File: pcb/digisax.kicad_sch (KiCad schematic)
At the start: 28 parts, among them U1 TLV320DAC3100_breakout, U2 MPXV7007, U3 ESP32-S3, U4 MCP3221

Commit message: completed first iteration of schem
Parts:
- removed key_HFS: SW_Push, symbol Switch:SW_Push
- added D10, D11, D12, D13, D14, D15, D16, D17, D18, D19, D2, D20, D21, D3, D4, D5, D6, D7, D8, D9: 1N4148, Diode_THT:D_DO-35_SOD27_P7.62mm_Horizontal, symbol Diode:1N4148
- added SW1: RotaryEncoder_Switch, symbol Device:RotaryEncoder_Switch
- added U5: ER_OLEDM0.91_1x-I2C, Display:ER_OLEDM0.91_1x-I2C, symbol Display_Graphic:ER_OLEDM0.91_1x-I2C
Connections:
- net +3.3V: now also U5.2 (VCC)
- net GND: now also SW1.C, SW1.S2, U5.1 (GND)
- net I2C_SCL: now also U5.3 (SCL)
- net I2C_SDA: now also U5.4 (SDA)
- net key_OCT: no longer key_L4.1
- net key_R1: now also D1.1 (K), U3.7 (GPIO7), D15.1 (K), D8.1 (K); no longer key_R1.1
- net key_R2: now also U3.8 (GPIO15), D16.1 (K), D2.1 (K), D9.1 (K); no longer key_R2.1
- net key_C2: now reaches key_BF1.2, key_L1.2, key_L2.2, key_L3.2, key_R1.2, key_R2.2, key_R3.2
- net key_C2: now also U3.17 (GPIO11)
- net key_C3: now reaches key_LS1.2, key_LS2.2, key_LS3.2
- net key_C3: now also U3.18 (GPIO12), key_CS.2, key_GS.2, key_LB.2, key_LBF.2
- net key_C1: now reaches key_C.2, key_DS.2
- net key_C1: now also U3.16 (GPIO10), key_L4.2, key_RS1.2, key_RS2.2, key_RS3.2, key_TR.2
- net key_R5: now reaches U3.10 (GPIO17)
- net key_R5: now also D11.1 (K), D18.1 (K), D4.1 (K)
- net key_R7: now reaches U3.11 (GPIO18)
- net key_R7: now also D12.1 (K), D19.1 (K), D5.1 (K)
- net key_R8: now reaches U3.12 (GPIO8)
- net key_R8: now also D13.1 (K), D20.1 (K), D6.1 (K)
- net key_R9: now reaches U3.15 (GPIO9)
- net key_R9: now also D14.1 (K), D21.1 (K), D7.1 (K)
- net EC11_A: now reaches U3.27 (GPIO2)
- net EC11_A: now also SW1.A
- net EC11_B: now reaches U3.28 (GPIO42)
- net EC11_B: now also SW1.B
- net key_R4: now reaches U3.9 (GPIO16)
- net key_R4: now also D10.1 (K), D17.1 (K), D3.1 (K)
- net at D1.2 (A): now also key_L4.1
- net key_BF: no longer names the net of key_BF1.1
- net key_BF: now also D9.2 (A)
- net key_C: no longer names the net of key_C.1
- net key_C: now also D6.2 (A)
- net key_CS: no longer names the net of key_CS.1
- net key_CS: now also D19.2 (A)
- net key_DS: no longer names the net of key_DS.1
- net key_DS: now also D5.2 (A)
- net key_GS: no longer names the net of key_GS.1
- net key_GS: now also D18.2 (A)
- net key_L1: no longer names the net of key_L1.1
- net key_L1: now also D8.2 (A)
- net key_L2: no longer names the net of key_L2.1
- net key_L2: now also D10.2 (A)
- net key_L3: no longer names the net of key_L3.1
- net key_L3: now also D11.2 (A)
- net key_LB: no longer names the net of key_LB.1
- net key_LB: now also D20.2 (A)
- net key_LBF: no longer names the net of key_LBF.1
- net key_LBF: now also D21.2 (A)
- net key_LS1: no longer names the net of key_LS1.1
- net key_LS1: now also D17.2 (A)
- net key_LS2: no longer names the net of key_LS2.1
- net key_LS2: now also D16.2 (A)
- net key_LS3: no longer names the net of key_LS3.1
- net key_LS3: now also D15.2 (A)
- net key_R3: no longer names the net of key_R3.1
- net key_R3: now also D14.2 (A)
- net key_RS1: no longer names the net of key_RS1.1
- net key_RS1: now also D4.2 (A)
- net key_RS2: no longer names the net of key_RS2.1
- net key_RS2: now also D3.2 (A)
- net key_RS3: no longer names the net of key_RS3.1
- net key_RS3: now also D2.2 (A)
- net key_TR: no longer names the net of key_TR.1
- net key_TR: now also D7.2 (A)
- new net: D13.2 (A), key_R2.1
- new net: D12.2 (A), key_R1.1
- new net EC11_button: SW1.S1
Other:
- note added: "DAC"
- note added: "Differential pressure sensor"
- note added: "Key matrix"
- note added: "MCU"
- note added: "OLED display"
- note added: "Rotary encoder"
- moved on the sheet: C1, D1, U1, U2, U3, U4, key_BF1, key_C, key_CS, key_DS, key_GS, key_L1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

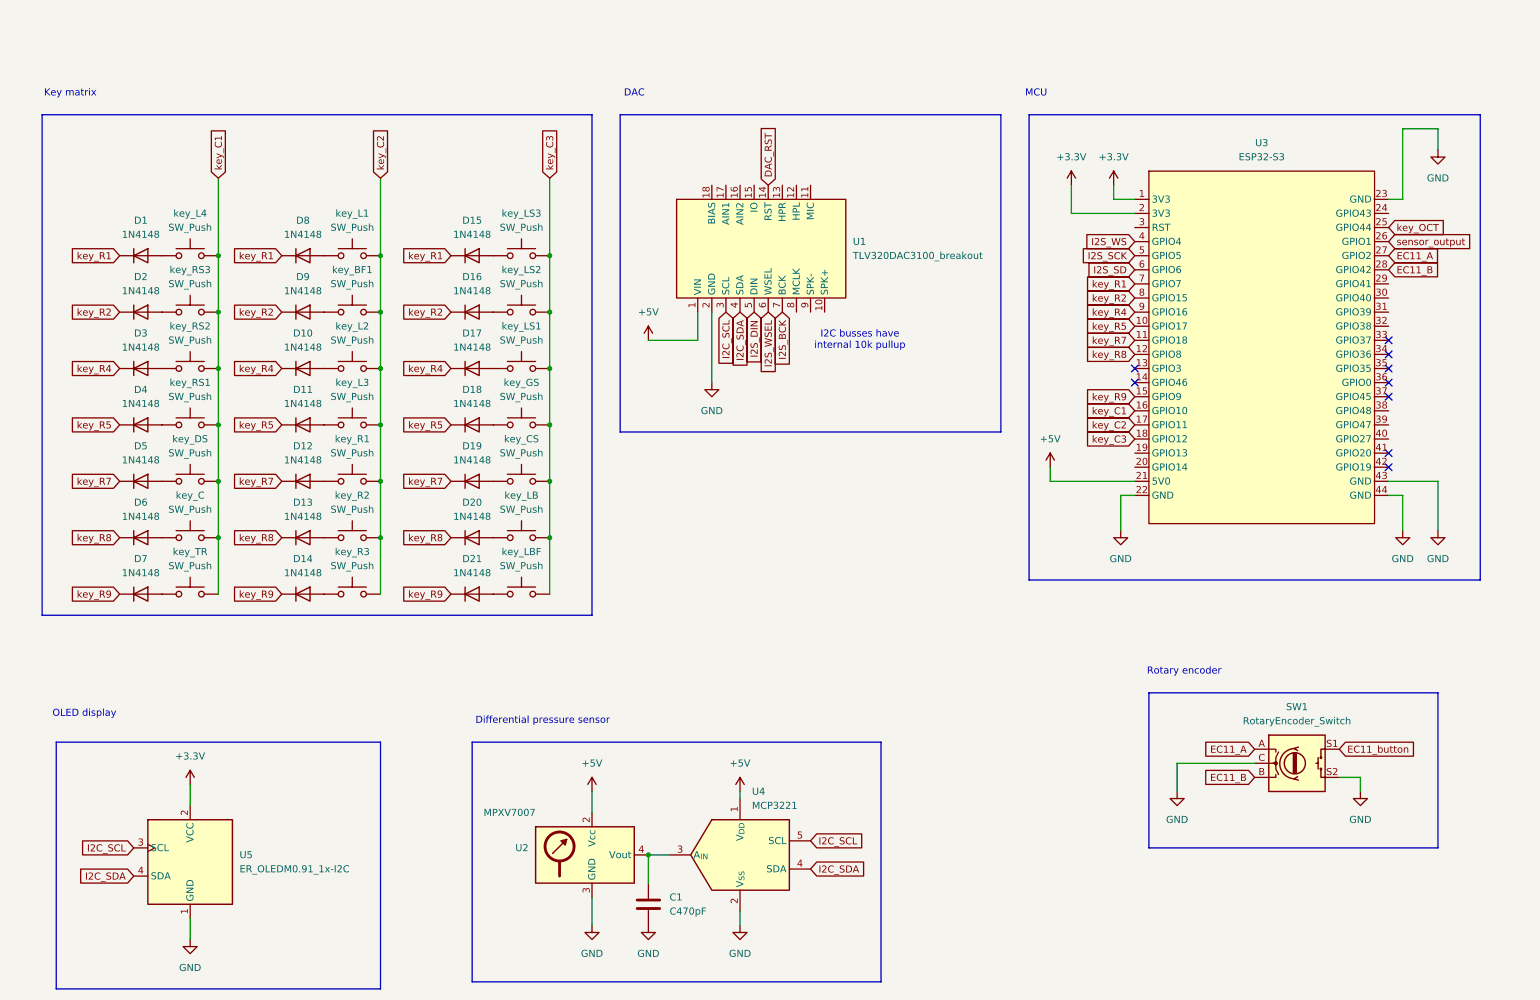
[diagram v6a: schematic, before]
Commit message: added decoupling caps
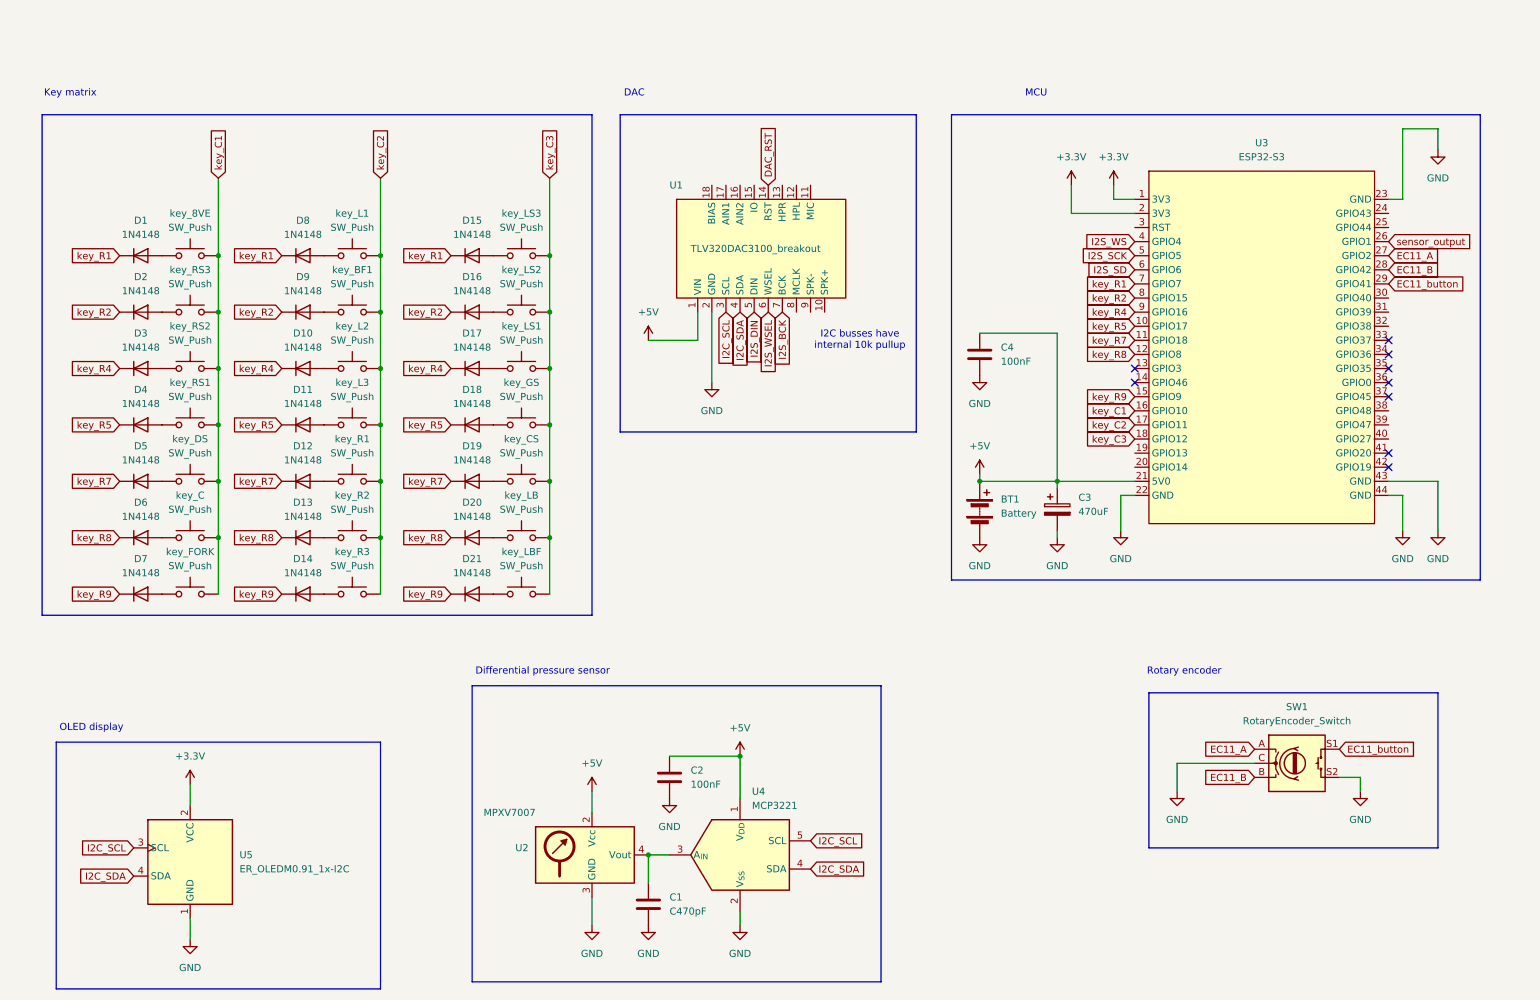
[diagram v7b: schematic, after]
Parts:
- added BT1: Battery, symbol Device:Battery
- added C2, C4: 100nF, symbol Device:C
- added C3: 470uF, symbol Device:C_Polarized
- renumbered key_L4 to key_8VE, key_TR to key_FORK
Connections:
- net +5V: now also BT1.1 (+), C2.1, C3.1, C4.1
- net EC11_button: now also U3.29 (GPIO41)
- net GND: now also BT1.2 (-), C2.2, C3.2, C4.2
- net key_OCT: no longer names the net of U3.25 (GPIO44)
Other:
- title: (none) -> Digisax

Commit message: completed footprints and 3d models
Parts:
- SW1: footprint (none) -> Rotary_Encoder:RotaryEncoder_Alps_EC11E-Switch_Vertical_H20mm
- U2: footprint (none) -> digisax_stuff:MPXV7007DP
- U4: renamed from U1; footprint (none) -> digisax_stuff:adafruit_TLV320DAC3100
- U5: renamed from U3; footprint (none) -> digisax_stuff:ESP32-S3-DevKitC-1
- key_8VE1: renamed from key_8VE; footprint (none) -> Button_Switch_Keyboard:SW_Cherry_MX_1.00u_PCB
- key_BF1, key_L1, key_L2, key_L3, key_LS2, key_R1, key_R2, key_R3, key_RS2: footprint (none) -> Button_Switch_Keyboard:SW_Cherry_MX_1.00u_PCB
- key_C1: renamed from key_C; footprint (none) -> Button_Switch_Keyboard:SW_Cherry_MX_1.00u_PCB
- key_CS1: renamed from key_CS; footprint (none) -> Button_Switch_Keyboard:SW_Cherry_MX_1.00u_PCB
- key_DS1: renamed from key_DS; footprint (none) -> Button_Switch_Keyboard:SW_Cherry_MX_1.00u_PCB
- key_FORK1: renamed from key_FORK; footprint (none) -> Button_Switch_Keyboard:SW_Cherry_MX_1.00u_PCB
- key_GS1: renamed from key_GS; footprint (none) -> Button_Switch_Keyboard:SW_Cherry_MX_1.00u_PCB
- key_LB1: renamed from key_LB; footprint (none) -> Button_Switch_Keyboard:SW_Cherry_MX_1.00u_PCB
- key_LBF1: renamed from key_LBF; footprint (none) -> Button_Switch_Keyboard:SW_Cherry_MX_1.00u_PCB
- key_LS1: renamed from key_LS3; footprint (none) -> Button_Switch_Keyboard:SW_Cherry_MX_1.00u_PCB
- key_LS3: renamed from key_LS1; footprint (none) -> Button_Switch_Keyboard:SW_Cherry_MX_1.00u_PCB
- key_RS1: renamed from key_RS3; footprint (none) -> Button_Switch_Keyboard:SW_Cherry_MX_1.00u_PCB
- key_RS3: renamed from key_RS1; footprint (none) -> Button_Switch_Keyboard:SW_Cherry_MX_1.00u_PCB
- renumbered C4 to C3, C3 to C4, U5 to U1, U4 to U3
